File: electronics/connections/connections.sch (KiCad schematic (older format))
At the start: 3 parts

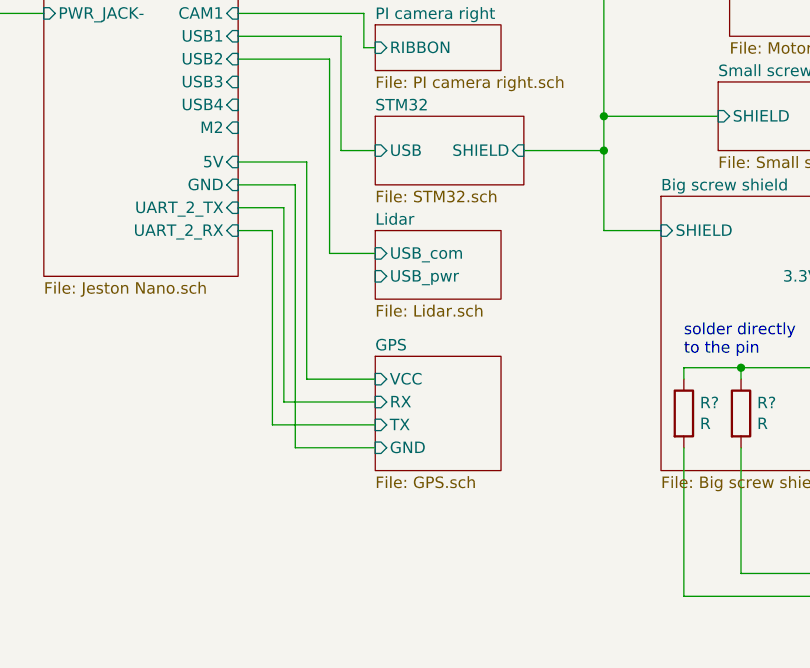
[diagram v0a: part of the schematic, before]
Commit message: Edit button panel, edit CAD, add motor tensioners
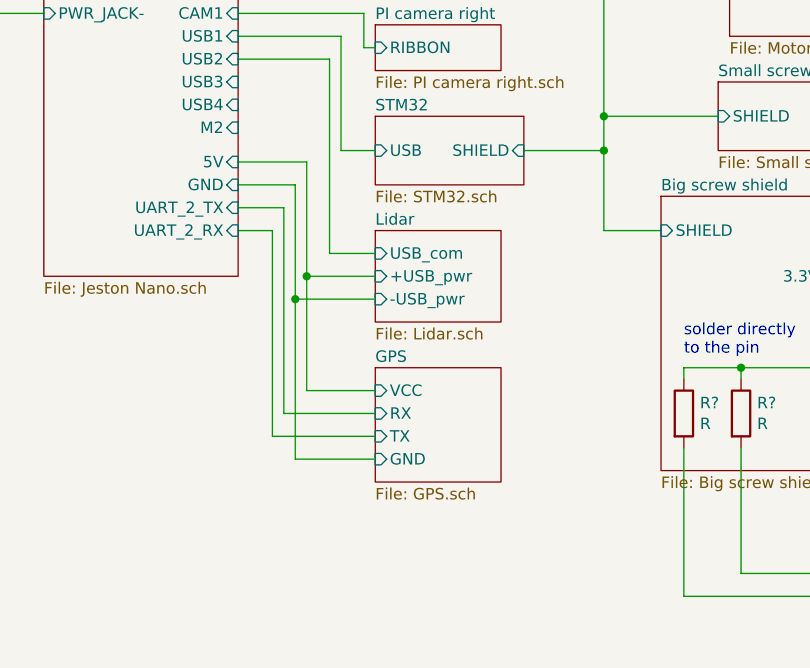
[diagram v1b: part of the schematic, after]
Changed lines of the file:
@@
 $EndSheet
 $Sheet
-S 6150 2900 550  300
+S 6150 2900 550  400
 U 6044A856
 F0 "Lidar" 50
 F1 "Lidar.sch" 50
 F2 "USB_com" I L 6150 3000 50
-F3 "USB_pwr" I L 6150 3100 50
+F3 "+USB_pwr" I L 6150 3100 50
+F4 "-USB_pwr" I L 6150 3200 50
 $EndSheet
 $Sheet
@@
 $EndSheet
 $Sheet
-S 6150 3450 550  500
+S 6150 3500 550  500
 U 6044AA86
 F0 "GPS" 50
 F1 "GPS.sch" 50
-F2 "VCC" I L 6150 3550 50
-F3 "RX" I L 6150 3650 50
-F4 "TX" I L 6150 3750 50
-F5 "GND" I L 6150 3850 50
+F2 "VCC" I L 6150 3600 50
+F3 "RX" I L 6150 3700 50
+F4 "TX" I L 6150 3800 50
+F5 "GND" I L 6150 3900 50
 $EndSheet
 $Sheet
@@
 	5550 2600 5850 2600
 Wire Wire Line
-	5850 2600 5850 3550
-Wire Wire Line
-	5850 3550 6150 3550
-Wire Wire Line
 	5550 2700 5800 2700
 Wire Wire Line
-	5800 2700 5800 3850
-Wire Wire Line
-	5800 3850 6150 3850
-Wire Wire Line
 	5550 2800 5750 2800
 Wire Wire Line
-	5750 2800 5750 3650
-Wire Wire Line
-	5750 3650 6150 3650
-Wire Wire Line
 	5550 2900 5700 2900
 Wire Wire Line
-	5700 2900 5700 3750
-Wire Wire Line
-	5700 3750 6150 3750
+	5850 3600 6150 3600
+Wire Wire Line
+	5850 2600 5850 3100
+Wire Wire Line
+	5750 3700 6150 3700
+Wire Wire Line
+	5750 2800 5750 3700
+Wire Wire Line
+	5700 3800 6150 3800
+Wire Wire Line
+	5700 2900 5700 3800
+Wire Wire Line
+	5800 3900 6150 3900
+Wire Wire Line
+	5800 2700 5800 3200
+Wire Wire Line
+	5850 3100 6150 3100
+Connection ~ 5850 3100
+Wire Wire Line
+	5850 3100 5850 3600
+Wire Wire Line
+	5800 3200 6150 3200
+Connection ~ 5800 3200
+Wire Wire Line
+	5800 3200 5800 3900
 $EndSCHEMATC

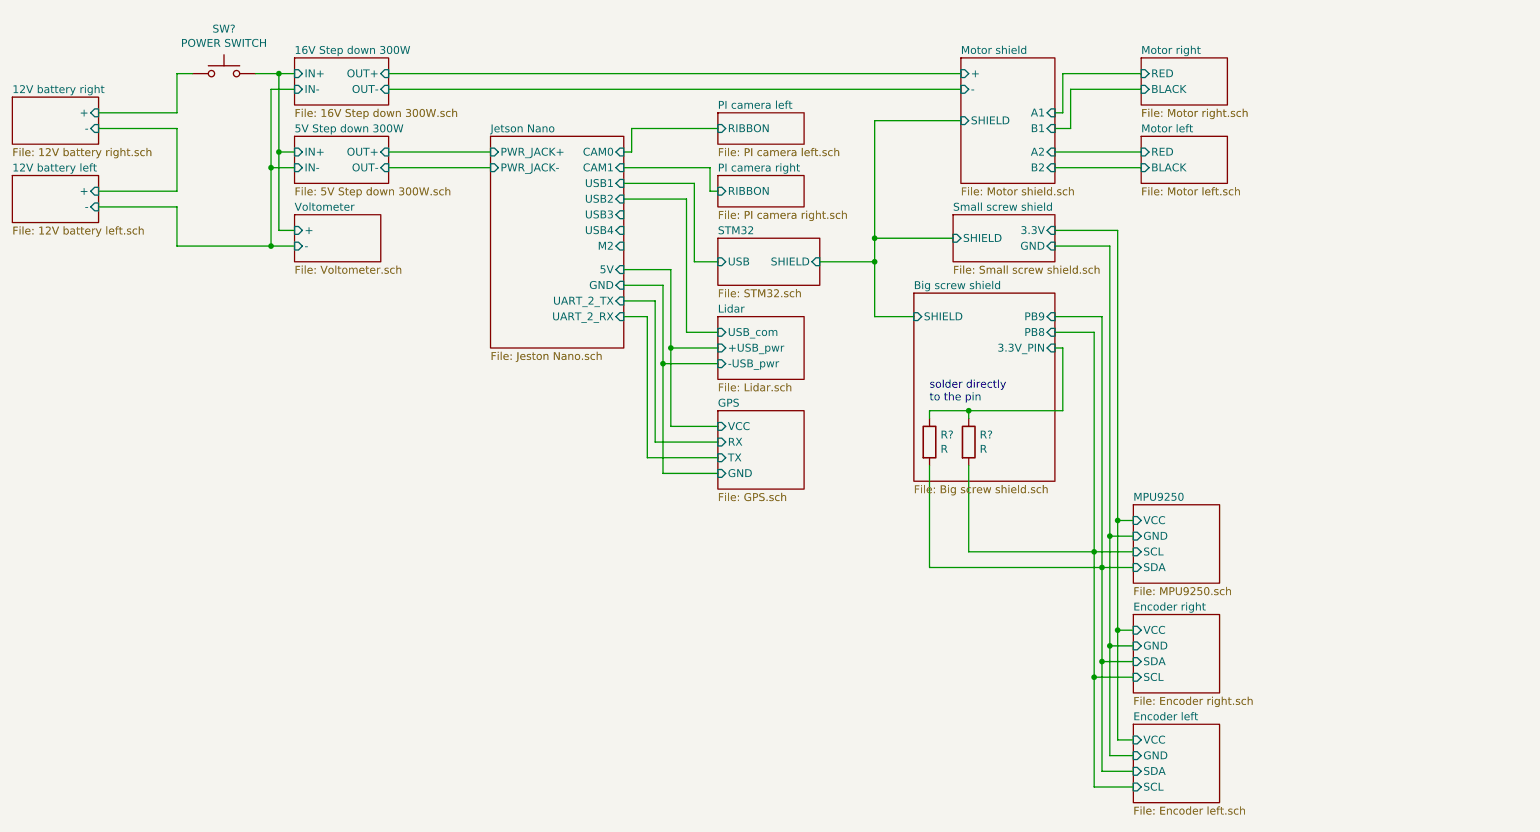
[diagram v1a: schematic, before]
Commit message: Add chain guide models
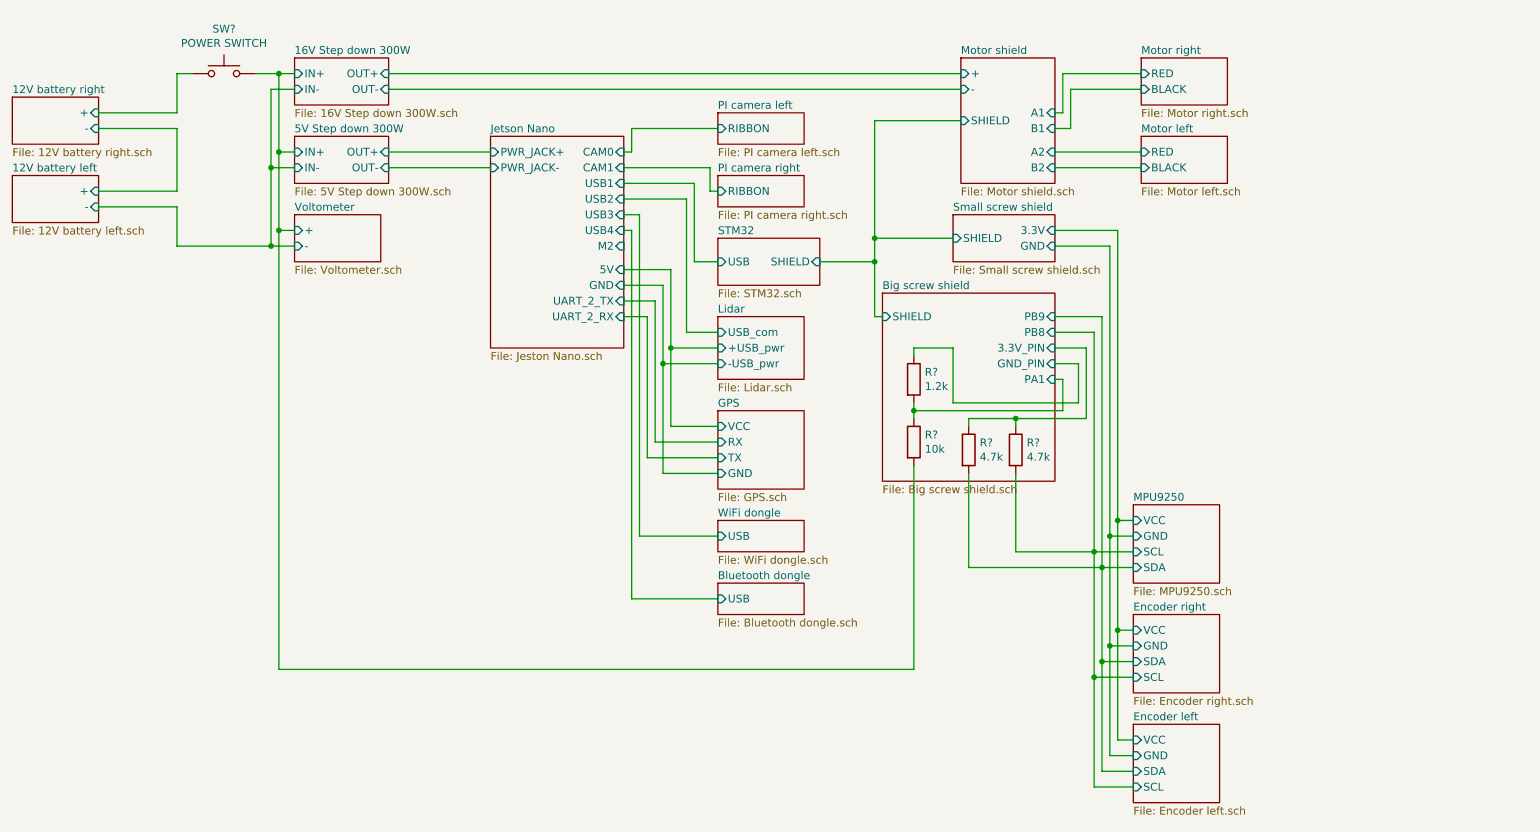
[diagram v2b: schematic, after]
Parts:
- added R?: 10k, symbol Device:R
- added R?: 1.2k, symbol Device:R
- R? (x2): value R -> 4.7k
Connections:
- net 16V Step down 300W/IN+: now also R?.2
- new net Big screw shield/GND_PIN: R?.1
- new net Big screw shield/PA1: R?.1, R?.2
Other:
- note removed: "solder directly \nto the pin"
- moved on the sheet: R?
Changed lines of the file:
@@
 $Descr A4 11693 8268
 encoding utf-8
-Sheet 1 20
+Sheet 1 22
 Title ""
 Date ""
@@
 L Device:R R?
 U 1 1 60456894
-P 7750 3700
-F 0 "R?" H 7820 3746 50  0000 L CNN
-F 1 "R" H 7820 3655 50  0000 L CNN
-F 2 "" V 7680 3700 50  0001 C CNN
-F 3 "~" H 7750 3700 50  0001 C CNN
-	1    7750 3700
+P 8050 3750
+F 0 "R?" H 8120 3796 50  0000 L CNN
+F 1 "4.7k" H 8120 3705 50  0000 L CNN
+F 2 "" V 7980 3750 50  0001 C CNN
+F 3 "~" H 8050 3750 50  0001 C CNN
+	1    8050 3750
 	1    0    0    -1
 $EndComp
@@
 L Device:R R?
 U 1 1 604570D2
-P 7500 3700
-F 0 "R?" H 7570 3746 50  0000 L CNN
-F 1 "R" H 7570 3655 50  0000 L CNN
-F 2 "" V 7430 3700 50  0001 C CNN
-F 3 "~" H 7500 3700 50  0001 C CNN
-	1    7500 3700
+P 7750 3750
+F 0 "R?" H 7820 3796 50  0000 L CNN
+F 1 "4.7k" H 7820 3705 50  0000 L CNN
+F 2 "" V 7680 3750 50  0001 C CNN
+F 3 "~" H 7750 3750 50  0001 C CNN
+	1    7750 3750
 	1    0    0    -1
 $EndComp
@@
 $EndSheet
 $Sheet
-S 7400 2750 900  1200
+S 7200 2750 1100 1200
 U 6045FAE0
 F0 "Big screw shield" 50
 F1 "Big screw shield.sch" 50
-F2 "SHIELD" I L 7400 2900 50
+F2 "SHIELD" I L 7200 2900 50
 F3 "PB9" I R 8300 2900 50
 F4 "PB8" I R 8300 3000 50
 F5 "3.3V_PIN" I R 8300 3100 50
+F6 "GND_PIN" I R 8300 3200 50
+F7 "PA1" I R 8300 3300 50
 $EndSheet
 $Sheet
@@
 F4 "GND" I R 8300 2450 50
 $EndSheet
-Text Notes 7500 3450 0    50   ~ 0
-solder directly \nto the pin
-Wire Wire Line
-	7500 3550 7500 3500
-Wire Wire Line
-	7500 3500 7750 3500
-Wire Wire Line
-	8350 3500 8350 3100
-Wire Wire Line
-	8350 3100 8300 3100
-Wire Wire Line
-	7750 3550 7750 3500
-Connection ~ 7750 3500
-Wire Wire Line
-	7750 3500 8350 3500
-Wire Wire Line
-	8550 4400 7750 4400
-Wire Wire Line
-	7750 4400 7750 3850
+Wire Wire Line
+	8550 4400 8050 4400
 Connection ~ 8550 4400
 Wire Wire Line
-	8600 4500 7500 4500
-Wire Wire Line
-	7500 4500 7500 3850
+	8600 4500 7750 4500
 Connection ~ 8600 4500
 Wire Wire Line
@@
 Wire Wire Line
 	7150 2400 7150 2550
-Wire Wire Line
-	7150 2900 7400 2900
 $Comp
 L Switch:SW_Push SW?
@@
 Wire Wire Line
 	5800 3200 5800 3900
+$Comp
+L Device:R R?
+U 1 1 60520E00
+P 7400 3700
+F 0 "R?" H 7470 3746 50  0000 L CNN
+F 1 "10k" H 7470 3655 50  0000 L CNN
+F 2 "" V 7330 3700 50  0001 C CNN
+F 3 "~" H 7400 3700 50  0001 C CNN
+	1    7400 3700
+	1    0    0    -1
+$EndComp
+$Comp
+L Device:R R?
+U 1 1 60521303
+P 7400 3300
+F 0 "R?" H 7470 3346 50  0000 L CNN
+F 1 "1.2k" H 7470 3255 50  0000 L CNN
+F 2 "" V 7330 3300 50  0001 C CNN
+F 3 "~" H 7400 3300 50  0001 C CNN
+	1    7400 3300
+	1    0    0    -1
+$EndComp
+Wire Wire Line
+	7150 2900 7200 2900
+Wire Wire Line
+	8300 3100 8500 3100
+Wire Wire Line
+	7400 3150 7400 3100
+Wire Wire Line
+	7400 3100 7650 3100
+Wire Wire Line
+	8450 3200 8300 3200
+Wire Wire Line
+	7750 4500 7750 3900
+Wire Wire Line
+	8500 3100 8500 3550
+Wire Wire Line
+	7750 3600 7750 3550
+Connection ~ 3350 2350
+Wire Wire Line
+	7750 3550 8050 3550
+Wire Wire Line
+	8050 3550 8050 3600
+Connection ~ 8050 3550
+Wire Wire Line
+	8050 3550 8500 3550
+Wire Wire Line
+	8050 3900 8050 4400
+Wire Wire Line
+	7400 3450 7400 3500
+Wire Wire Line
+	7400 3500 8350 3500
+Wire Wire Line
+	8350 3500 8350 3300
+Wire Wire Line
+	8350 3300 8300 3300
+Connection ~ 7400 3500
+Wire Wire Line
+	7400 3500 7400 3550
+Wire Wire Line
+	7650 3450 8450 3450
+Wire Wire Line
+	8450 3200 8450 3450
+Wire Wire Line
+	7650 3100 7650 3450
+$Sheet
+S 6150 4200 550  200
+U 6056CA13
+F0 "WiFi dongle" 50
+F1 "WiFi dongle.sch" 50
+F2 "USB" I L 6150 4300 50
+$EndSheet
+$Sheet
+S 6150 4600 550  200
+U 6056CA78
+F0 "Bluetooth dongle" 50
+F1 "Bluetooth dongle.sch" 50
+F2 "USB" I L 6150 4700 50
+$EndSheet
+Wire Wire Line
+	5550 2250 5650 2250
+Wire Wire Line
+	5650 2250 5650 4300
+Wire Wire Line
+	5550 2350 5600 2350
+Wire Wire Line
+	5600 2350 5600 4700
+Wire Wire Line
+	6150 4300 5650 4300
+Wire Wire Line
+	6150 4700 5600 4700
+Wire Wire Line
+	7400 5150 3350 5150
+Wire Wire Line
+	7400 3850 7400 5150
+Wire Wire Line
+	3350 2350 3350 5150
 $EndSCHEMATC

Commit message: Change connections
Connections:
- net Big screw shield/PA1 renamed Big screw shield/PC0
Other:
- note added: "Add ferrite bead close to the motor shield"
- note added: "Remove 10k pull ups on SDA / SCL pins"
- note added: "Solder jumper close to voltage regulator"
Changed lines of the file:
@@
 F5 "3.3V_PIN" I R 8300 3100 50
 F6 "GND_PIN" I R 8300 3200 50
-F7 "PA1" I R 8300 3300 50
+F7 "PC0" I R 8300 3300 50
 $EndSheet
 $Sheet
@@
 Wire Wire Line
 	3350 2350 3350 5150
+Wire Notes Line
+	8450 2000 8750 2000
+Wire Notes Line
+	8750 2000 8750 1300
+Wire Notes Line
+	8750 1300 8450 1300
+Wire Notes Line
+	8450 1300 8450 2000
+Text Notes 7850 1050 0    50   ~ 0
+Add ferrite bead close to the motor shield
+Wire Notes Line
+	8600 1300 8600 1100
+Text Notes 9400 4200 0    50   ~ 0
+Solder jumper close to voltage regulator
+Text Notes 9400 4300 0    50   ~ 0
+Remove 10k pull ups on SDA / SCL pins
 $EndSCHEMATC
